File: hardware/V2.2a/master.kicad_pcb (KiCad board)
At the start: 4 copper layers, 40 x 40 mm, 115 parts, among them J101 USB-MINI-B-SMD, J102 DRILL, J103 DRILL, J104 DRILL, J105 DRILL, J301 STACK-UP-LOW, J302 STACK-DOWN, J303 STACK-UP-LOW, J304 STACK-DOWN, P201 CON-SENSOR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

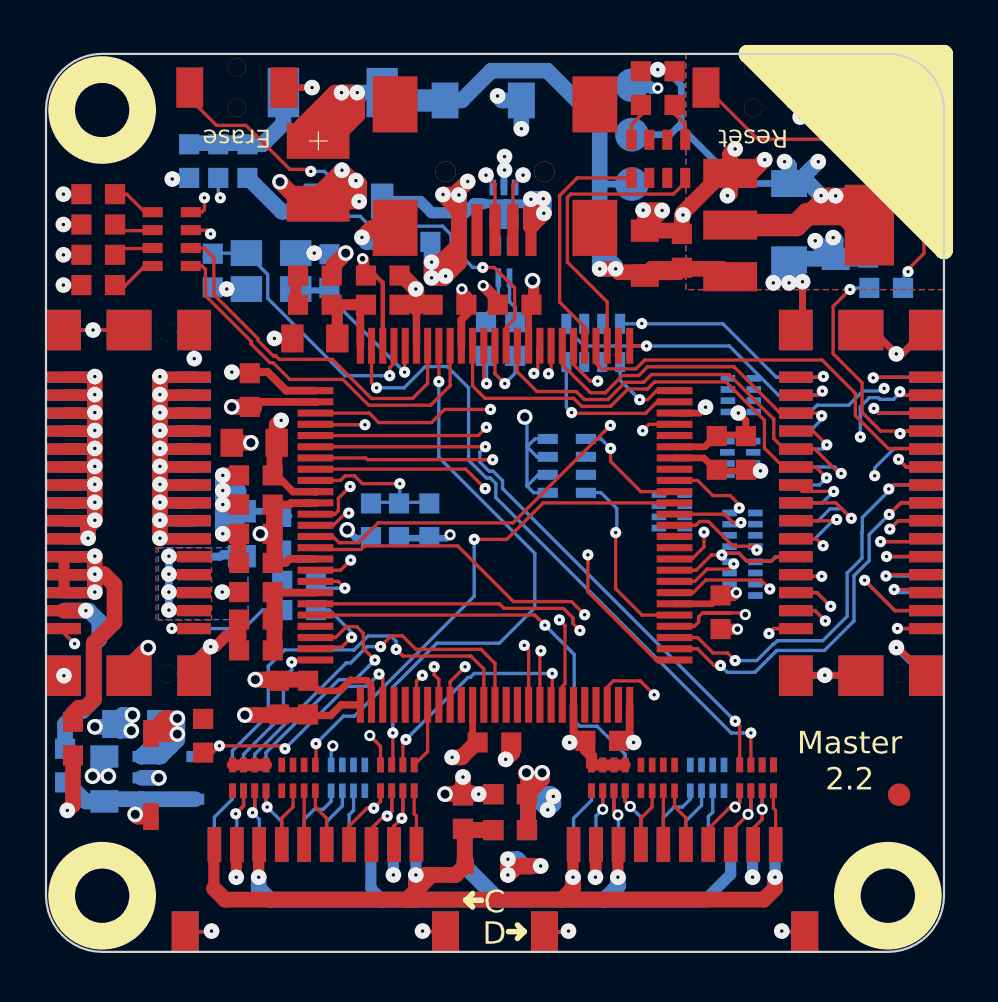
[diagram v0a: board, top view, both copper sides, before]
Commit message: new master brick prototype finished
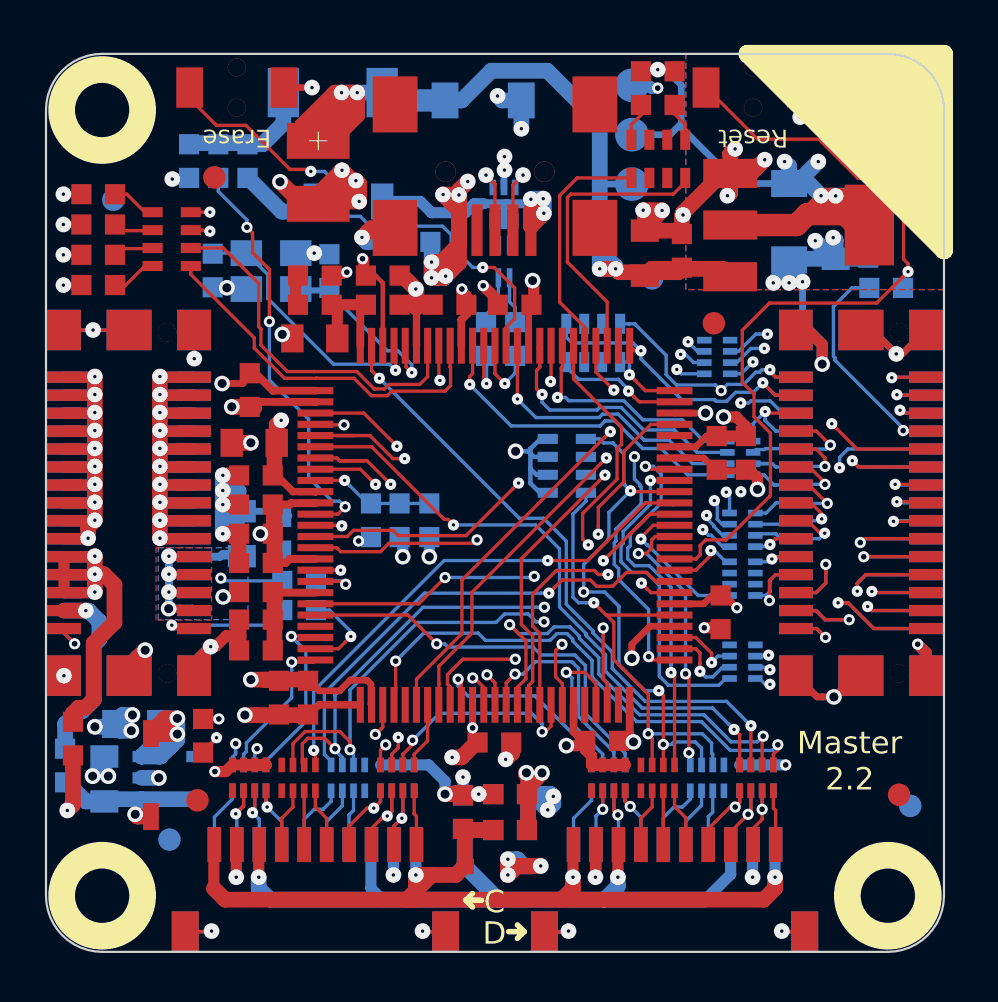
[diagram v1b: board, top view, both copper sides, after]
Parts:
- removed the G*** at (142.3, 86.4)
- added Fiducial_Mark: VAL**, kicad-libraries:Fiducial_Mark, F.Cu at (134.8, 80.4)
- added Fiducial_Mark: VAL**, kicad-libraries:Fiducial_Mark, F.Cu at (134.1, 108.2)
- added Fiducial_Mark: VAL**, kicad-libraries:Fiducial_Mark, F.Cu at (157.1, 86.9)
- added Fiducial_Mark: VAL**, kicad-libraries:Fiducial_Mark, B.Cu at (165.8, 108.4)
- added Fiducial_Mark: VAL**, kicad-libraries:Fiducial_Mark, B.Cu at (132.8, 109.9)
- added Fiducial_Mark: VAL**, kicad-libraries:Fiducial_Mark, B.Cu at (130.3, 81.4)
- added Fiducial_Mark: VAL**, kicad-libraries:Fiducial_Mark, B.Cu at (154.3, 84.9)
- added G***: Logo_31x31, kicad-libraries:Logo_31x31, B.Cu at (142.1, 86.4)
- added G***: LOGO, kicad-libraries:WEEE_7mm, B.Cu at (153.8, 101.7)
- added VAL: CE_5mm, kicad-libraries:CE_5mm, B.Cu at (142.8, 102.9)
- F101: footprint 1206 -> kicad-libraries:1206
- moved RP305 7.40 mm to (158.3, 102.0)
- moved RP302 2.00 mm to (157.2, 88.4)
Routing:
- net BRICKLET-I2C-SDA: track 5.26 -> 42.7 mm, vias 1 -> 6
- net GND: track 420.9 -> 456.5 mm, vias 74 -> 79
- net BRICKLET-I2C-SCL: track 8.37 -> 41.7 mm, vias 1 -> 4
- net BRICKLET-IO3_3: track 0.00 -> 23.5 mm, vias 0 -> 2
- net BRICKLET-IO3_2/PWM3: track 0.00 -> 19.6 mm, vias 0 -> 2
- net Net-(C413-Pad1): track 76.6 -> 94.8 mm, vias 4 -> 6
- net BRICKLET-SEL-3: track 0.00 -> 17.0 mm, vias 0 -> 2
- net STACK-SELECT-EX-00: track 17.1 -> 3.14 mm, vias 2 -> 1
- net Net-(J301-Pad17): track 2.48 -> 16.0 mm, vias 0 -> 2
- net BRICKLET-SEL-1: track 0.00 -> 12.7 mm, vias 0 -> 3
- net Net-(J303-Pad30): track 3.16 -> 14.3 mm, vias 1 -> 2
- net BRICKLET-IO1_1: track 0.00 -> 9.67 mm, vias 0 -> 1
- net Net-(J301-Pad13): track 7.06 -> 16.5 mm, vias 1 -> 2
- net BRICKLET-IO1_3: track 0.00 -> 9.23 mm, vias 0 -> 1
- net Net-(J301-Pad15): track 7.09 -> 16.1 mm, vias 1 -> 2
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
